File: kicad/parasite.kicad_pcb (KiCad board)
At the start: 2 copper layers, 22 x 126.4 mm, 29 parts, among them Q1 2N3906, Q4 Q_Photo_NPN, U1 E73-2G4M08S1C, U2 SHTC3, Y1 32.768kHz

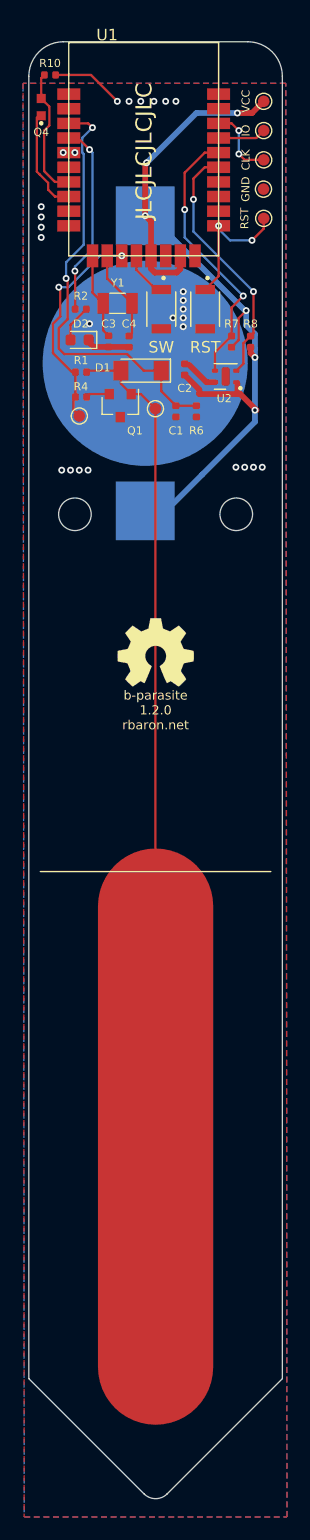
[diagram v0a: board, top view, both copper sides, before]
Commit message: Adds sketch of RC circuit in silkscreen
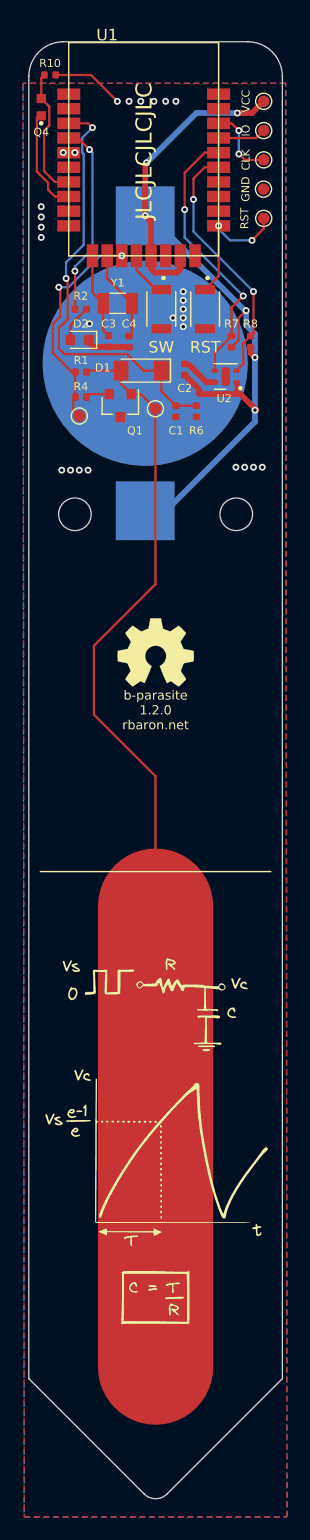
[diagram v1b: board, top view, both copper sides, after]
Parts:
- added G***: LOGO, drawing:circuit_drawing, F.Cu at (68.0, 122.2)
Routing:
- net CPARA: track 91.2 -> 95.6 mm

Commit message: Slightly better routing
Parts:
- U1: footprint snapeda:E73-2G4M08S1C-modified -> snapeda:E73-2G4M08S1C
- moved BT1 0.26 mm to (67.1, 55.2)
- renumbered S1 to RST, S2 to SW1
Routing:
- net +3V0: track 72.3 -> 76.5 mm, vias 6 -> 8
- net GND: track 13.1 -> 16.8 mm, vias 27 -> 29
- net SDA: track 24.0 -> 24.5 mm

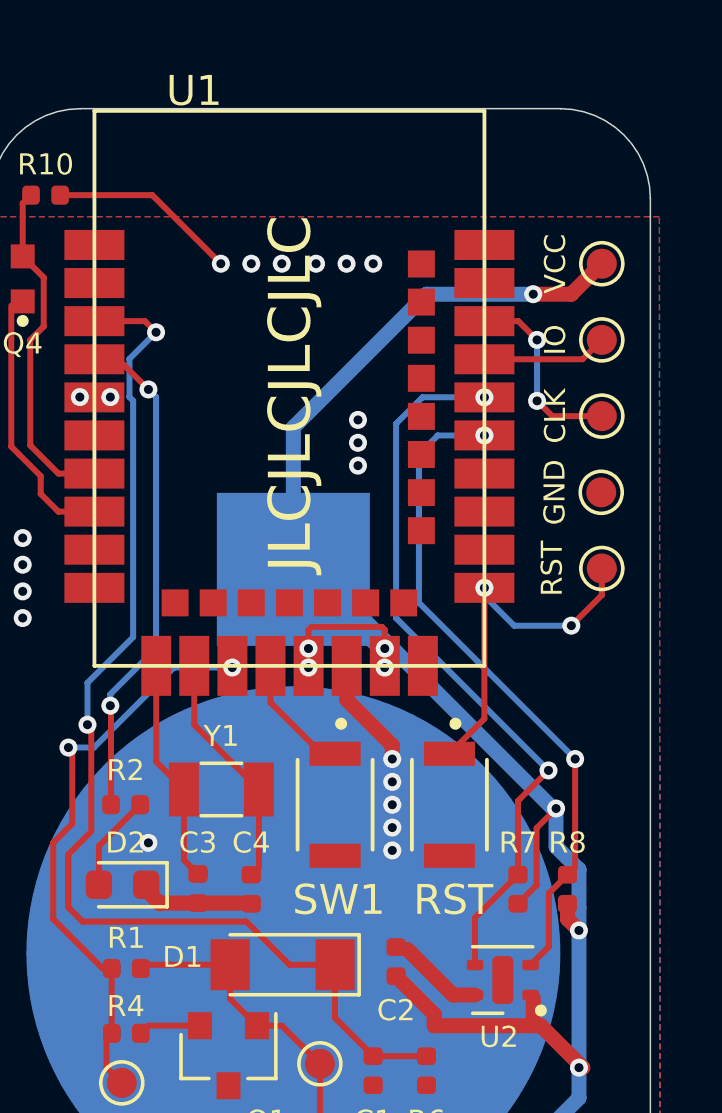
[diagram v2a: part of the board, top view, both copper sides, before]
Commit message: Routed 0.10 to a new test pad
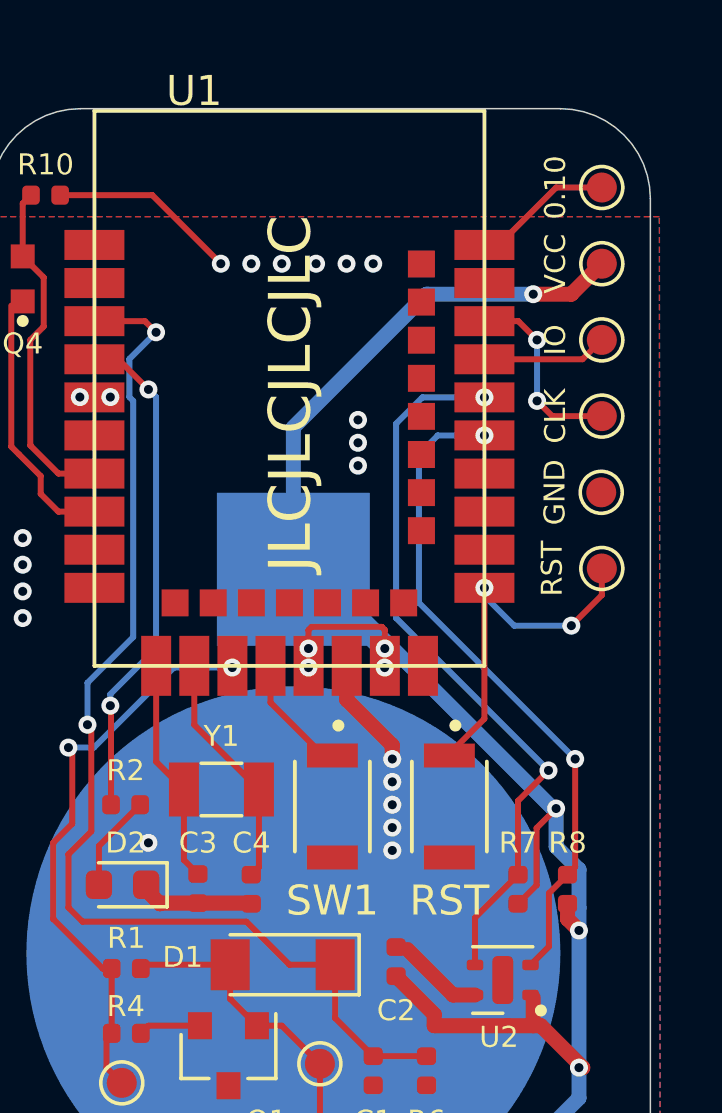
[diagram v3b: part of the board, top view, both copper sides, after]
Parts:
- removed RST, SW1: B3U-1000P, snapeda:SW_B3U-1000P
- added S1: B3U-1000P, snapeda:SW_B3U-1000P, F.Cu at (72.3, 50.3)
- added S2: B3U-1000P, snapeda:SW_B3U-1000P, F.Cu at (68.4, 50.3)
- added TP8: 0.10, TestPoint:TestPoint_Pad_D1.0mm, F.Cu at (77.4, 29.6)
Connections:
- U1 pad 43: unconnected-(U1-Pad43) -> 0.10
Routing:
- net 0.10: track 0.00 -> 4.71 mm
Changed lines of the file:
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@@
   (net 27 "unconnected-(U1-Pad31)")
   (net 28 "unconnected-(U1-Pad41)")
-  (net 29 "unconnected-(U1-Pad43)")
+  (net 29 "0.10")
   (net 30 "unconnected-(U2-Pad5)")
   (net 31 "unconnected-(U1-Pad12)")
@@
       (net 44 "unconnected-(U1-Pad42)") (pinfunction "P1.06") (pintype "bidirectional+no_connect"))
     (pad "43" smd rect (at 6.5 -5.03) (size 2 1) (layers "F.Cu" "F.Paste" "F.Mask")
-      (net 29 "unconnected-(U1-Pad43)") (pinfunction "P0.10/NFC2") (pintype "bidirectional+no_connect"))
+      (net 29 "0.10") (pinfunction "P0.10/NFC2") (pintype "bidirectional"))
     (model "${KIPRJMOD}/lib/snapeda/E73-2G4M08S1C.step"
       (offset (xyz 6.5 -9 0))
@@
   )
   (footprint "snapeda:SW_B3U-1000P" (layer "F.Cu")
-    (at 68.492 50.202 -90)
+    (at 68.4 50.2625 -90)
     (property "AVAILABILITY" "Unavailable")
     (property "DESCRIPTION" "Tactile Switch SPST-NO Top Actuated Surface Mount")
@@
     (property "Sheetname" "")
     (attr through_hole)
-    (fp_text reference "SW1" (at 3.175 -0.127) (layer "F.SilkS")
+    (fp_text reference "S2" (at 0.475 -2.335 90) (layer "F.SilkS") hide
       (effects (font (size 1 1) (thickness 0.15)))
     )
-    (fp_text value "B3U-1000P" (at 4.92 2.265 -90) (layer "F.Fab")
+    (fp_text value "B3U-1000P" (at 4.92 2.265 90) (layer "F.Fab") hide
+      (effects (font (size 1 1) (thickness 0.15)))
+    )
+    (fp_text user "SW1" (at 3.1375 0 unlocked) (layer "F.SilkS")
       (effects (font (size 1 1) (thickness 0.15)))
     )
-    (fp_line (start -1.5 -1.25) (end 1.5 -1.25) (layer "F.SilkS") (width 0.127))
     (fp_line (start -1.5 1.25) (end 1.5 1.25) (layer "F.SilkS") (width 0.127))
+    (fp_line (start -1.5 -1.25) (end 1.5 -1.25) (layer "F.SilkS") (width 0.127))
     (fp_circle (center -2.7 -0.2) (end -2.6 -0.2) (layer "F.SilkS") (width 0.2) (fill none))
-    (fp_line (start -2.35 1.1) (end -2.35 -1.1) (layer "F.CrtYd") (width 0.05))
-    (fp_line (start 1.75 -1.5) (end 1.75 -1.1) (layer "F.CrtYd") (width 0.05))
-    (fp_line (start -1.75 -1.5) (end 1.75 -1.5) (layer "F.CrtYd") (width 0.05))
+    (fp_line (start 1.75 1.1) (end 1.75 1.5) (layer "F.CrtYd") (width 0.05))
+    (fp_line (start -1.75 1.1) (end -2.35 1.1) (layer "F.CrtYd") (width 0.05))
+    (fp_line (start 1.75 1.5) (end -1.75 1.5) (layer "F.CrtYd") (width 0.05))
     (fp_line (start -1.75 -1.1) (end -1.75 -1.5) (layer "F.CrtYd") (width 0.05))
     (fp_line (start 2.35 -1.1) (end 2.35 1.1) (layer "F.CrtYd") (width 0.05))
-    (fp_line (start 1.75 -1.1) (end 2.35 -1.1) (layer "F.CrtYd") (width 0.05))
-    (fp_line (start 2.35 1.1) (end 1.75 1.1) (layer "F.CrtYd") (width 0.05))
+    (fp_line (start -2.35 1.1) (end -2.35 -1.1) (layer "F.CrtYd") (width 0.05))
+    (fp_line (start -1.75 -1.5) (end 1.75 -1.5) (layer "F.CrtYd") (width 0.05))
     (fp_line (start -2.35 -1.1) (end -1.75 -1.1) (layer "F.CrtYd") (width 0.05))
-    (fp_line (start 1.75 1.5) (end -1.75 1.5) (layer "F.CrtYd") (width 0.05))
-    (fp_line (start -1.75 1.1) (end -2.35 1.1) (layer "F.CrtYd") (width 0.05))
-    (fp_line (start 1.75 1.1) (end 1.75 1.5) (layer "F.CrtYd") (width 0.05))
+    (fp_line (start 1.75 -1.5) (end 1.75 -1.1) (layer "F.CrtYd") (width 0.05))
+    (fp_line (start 2.35 1.1) (end 1.75 1.1) (layer "F.CrtYd") (width 0.05))
     (fp_line (start -1.75 1.5) (end -1.75 1.1) (layer "F.CrtYd") (width 0.05))
+    (fp_line (start 1.75 -1.1) (end 2.35 -1.1) (layer "F.CrtYd") (width 0.05))
     (fp_line (start 1.5 1.25) (end -1.5 1.25) (layer "F.Fab") (width 0.127))
+    (fp_line (start 1.5 -1.25) (end -1.5 -1.25) (layer "F.Fab") (width 0.127))
     (fp_line (start 1.5 -1.25) (end 1.5 1.25) (layer "F.Fab") (width 0.127))
     (fp_line (start -1.5 1.25) (end -1.5 -1.25) (layer "F.Fab") (width 0.127))
-    (fp_line (start 1.5 -1.25) (end -1.5 -1.25) (layer "F.Fab") (width 0.127))
     (fp_circle (center -2.7 -0.2) (end -2.6 -0.2) (layer "F.Fab") (width 0.2) (fill none))
     (pad "1" smd rect locked (at -1.7 0) (size 1.7 0.8) (layers "F.Cu" "F.Paste" "F.Mask")
@@
   )
   (footprint "snapeda:SW_B3U-1000P" (layer "F.Cu")
-    (at 72.302 50.202 -90)
+    (at 72.3 50.2625 -90)
     (property "AVAILABILITY" "Unavailable")
     (property "DESCRIPTION" "Tactile Switch SPST-NO Top Actuated Surface Mount")
@@
     (property "Sheetname" "")
     (attr through_hole)
-    (fp_text reference "RST" (at 3.175 -0.127) (layer "F.SilkS")
+    (fp_text reference "S1" (at 0.475 -2.335 90) (layer "F.SilkS") hide
+      (effects (font (size 1 1) (thickness 0.15)))
+    )
+    (fp_text value "B3U-1000P" (at 4.92 2.265 90) (layer "F.Fab") hide
       (effects (font (size 1 1) (thickness 0.15)))
     )
-    (fp_text value "B3U-1000P" (at 4.92 2.265 -90) (layer "F.Fab")
+    (fp_text user "RST" (at 3.1375 0 unlocked) (layer "F.SilkS")
       (effects (font (size 1 1) (thickness 0.15)))
     )
@@
     (fp_line (start -1.5 -1.25) (end 1.5 -1.25) (layer "F.SilkS") (width 0.127))
     (fp_circle (center -2.7 -0.2) (end -2.6 -0.2) (layer "F.SilkS") (width 0.2) (fill none))
-    (fp_line (start 1.75 1.1) (end 1.75 1.5) (layer "F.CrtYd") (width 0.05))
     (fp_line (start -2.35 -1.1) (end -1.75 -1.1) (layer "F.CrtYd") (width 0.05))
-    (fp_line (start -2.35 1.1) (end -2.35 -1.1) (layer "F.CrtYd") (width 0.05))
-    (fp_line (start -1.75 1.1) (end -2.35 1.1) (layer "F.CrtYd") (width 0.05))
-    (fp_line (start 2.35 1.1) (end 1.75 1.1) (layer "F.CrtYd") (width 0.05))
+    (fp_line (start 1.75 -1.1) (end 2.35 -1.1) (layer "F.CrtYd") (width 0.05))
     (fp_line (start -1.75 -1.5) (end 1.75 -1.5) (layer "F.CrtYd") (width 0.05))
-    (fp_line (start -1.75 -1.1) (end -1.75 -1.5) (layer "F.CrtYd") (width 0.05))
-    (fp_line (start 2.35 -1.1) (end 2.35 1.1) (layer "F.CrtYd") (width 0.05))
-    (fp_line (start 1.75 -1.5) (end 1.75 -1.1) (layer "F.CrtYd") (width 0.05))
+    (fp_line (start -2.35 1.1) (end -2.35 -1.1) (layer "F.CrtYd") (width 0.05))
     (fp_line (start -1.75 1.5) (end -1.75 1.1) (layer "F.CrtYd") (width 0.05))
     (fp_line (start 1.75 1.5) (end -1.75 1.5) (layer "F.CrtYd") (width 0.05))
-    (fp_line (start 1.75 -1.1) (end 2.35 -1.1) (layer "F.CrtYd") (width 0.05))
-    (fp_line (start -1.5 1.25) (end -1.5 -1.25) (layer "F.Fab") (width 0.127))
+    (fp_line (start 1.75 -1.5) (end 1.75 -1.1) (layer "F.CrtYd") (width 0.05))
+    (fp_line (start 2.35 1.1) (end 1.75 1.1) (layer "F.CrtYd") (width 0.05))
+    (fp_line (start -1.75 1.1) (end -2.35 1.1) (layer "F.CrtYd") (width 0.05))
+    (fp_line (start 2.35 -1.1) (end 2.35 1.1) (layer "F.CrtYd") (width 0.05))
+    (fp_line (start -1.75 -1.1) (end -1.75 -1.5) (layer "F.CrtYd") (width 0.05))
+    (fp_line (start 1.75 1.1) (end 1.75 1.5) (layer "F.CrtYd") (width 0.05))
+    (fp_line (start 1.5 -1.25) (end -1.5 -1.25) (layer "F.Fab") (width 0.127))
     (fp_line (start 1.5 -1.25) (end 1.5 1.25) (layer "F.Fab") (width 0.127))
     (fp_line (start 1.5 1.25) (end -1.5 1.25) (layer "F.Fab") (width 0.127))
-    (fp_line (start 1.5 -1.25) (end -1.5 -1.25) (layer "F.Fab") (width 0.127))
+    (fp_line (start -1.5 1.25) (end -1.5 -1.25) (layer "F.Fab") (width 0.127))
     (fp_circle (center -2.7 -0.2) (end -2.6 -0.2) (layer "F.Fab") (width 0.2) (fill none))
     (pad "1" smd rect locked (at -1.7 0) (size 1.7 0.8) (layers "F.Cu" "F.Paste" "F.Mask")
@@
   )
   (footprint "TestPoint:TestPoint_Pad_D1.0mm" (layer "F.Cu")
+    (at 77.382 29.628 -90)
+    (descr "SMD pad as test Point, diameter 1.0mm")
+    (tags "test point SMD pad")
+    (property "Sheetfile" "parasite.kicad_sch")
+    (property "Sheetname" "")
+    (property "exclude_from_bom" "")
+    (attr exclude_from_pos_files exclude_from_bom)
+    (fp_text reference "TP8" (at 0 -1.448 90) (layer "F.SilkS") hide
+      (effects (font (size 1 1) (thickness 0.15)))
+    )
+    (fp_text value "0.10" (at 0 1.55 90) (layer "F.SilkS")
+      (effects (font (size 0.7 0.7) (thickness 0.12)))
+    )
+    (fp_text user "${REFERENCE}" (at 0 -1.45 90) (layer "F.Fab") hide
+      (effects (font (size 1 1) (thickness 0.15)))
+    )
+    (fp_circle (center 0 0) (end 0 0.7) (layer "F.SilkS") (width 0.12) (fill none))
+    (fp_circle (center 0 0) (end 1 0) (layer "F.CrtYd") (width 0.05) (fill none))
+    (pad "1" smd circle locked (at 0 0 270) (size 1 1) (layers "F.Cu" "F.Mask")
+      (net 29 "0.10") (pinfunction "1") (pintype "passive"))
+  )
+  (footprint "TestPoint:TestPoint_Pad_D1.0mm" (layer "F.Cu")
     (at 77.362 39.788 -90)
     (descr "SMD pad as test Point, diameter 1.0mm")
@@
   (via (at 75.223 34.708) (size 0.6) (drill 0.3) (layers "F.Cu" "B.Cu") (net 18))
   (segment (start 75.223 36.74) (end 75.223 34.708) (width 0.2) (layer "B.Cu") (net 18))
+  (segment (start 73.94345 31.54255) (end 75.858 29.628) (width 0.2) (layer "F.Cu") (net 29))
+  (segment (start 73.468 31.54255) (end 73.94345 31.54255) (width 0.2) (layer "F.Cu") (net 29))
+  (segment (start 75.858 29.628) (end 77.382 29.628) (width 0.2) (layer "F.Cu") (net 29))
   (zone (net 1) (net_name "GND") (layer "F.Cu") (hatch edge 0.508)
     (connect_pads (clearance 0.508))

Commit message: Fix drawing
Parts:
- removed the G*** at (68.0, 122.2)
- added G***: LOGO, b-parasite:circuit_drawing, F.Cu at (68.0, 120.1)
